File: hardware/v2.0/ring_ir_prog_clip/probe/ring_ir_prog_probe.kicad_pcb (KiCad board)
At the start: 2 copper layers, 14 x 29 mm, 11 parts, among them J1 AVR_ISP_6, J2 GND_lead_to_anvil, P1 Pogo TP1 PB0, P2 Pogo TP2 PB1, P3 Pogo TP3 PB2, P4 Pogo TP4 PB3, P5 Pogo TP5 PB4, P6 Pogo TP6 PB5, P9 Pogo TP9 VCC

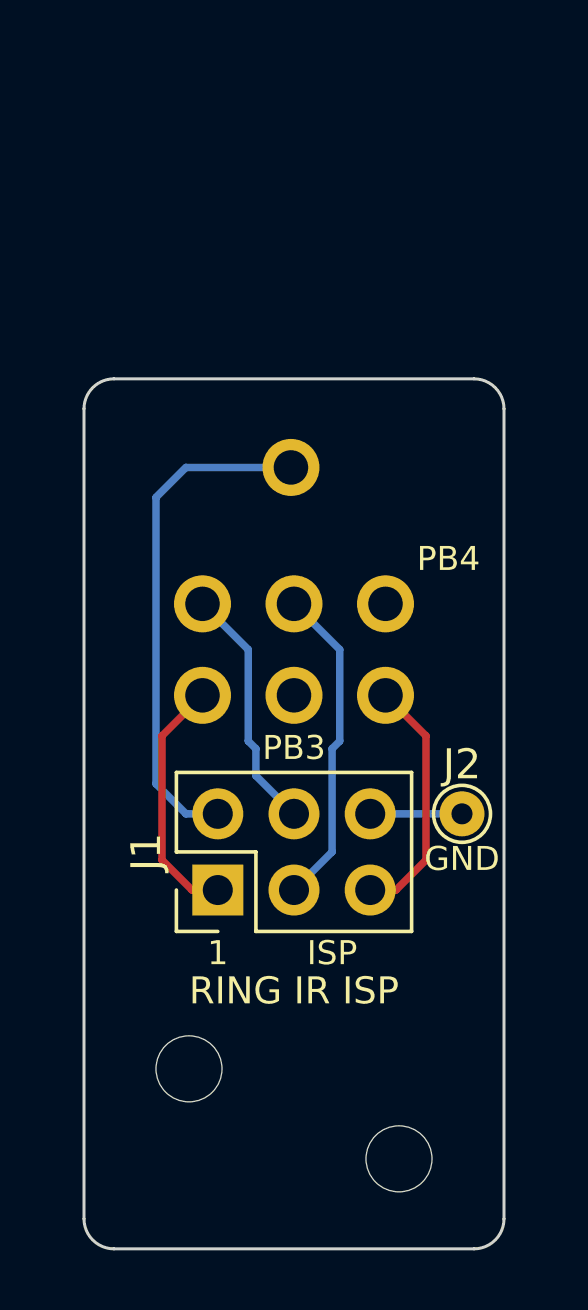
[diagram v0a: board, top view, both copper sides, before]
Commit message: IR prog clip: estimated clip dimensions and FreeCAD virtual fit check
Co-authored-by: Copilot <223556219+Copilot@users.noreply.github.com>
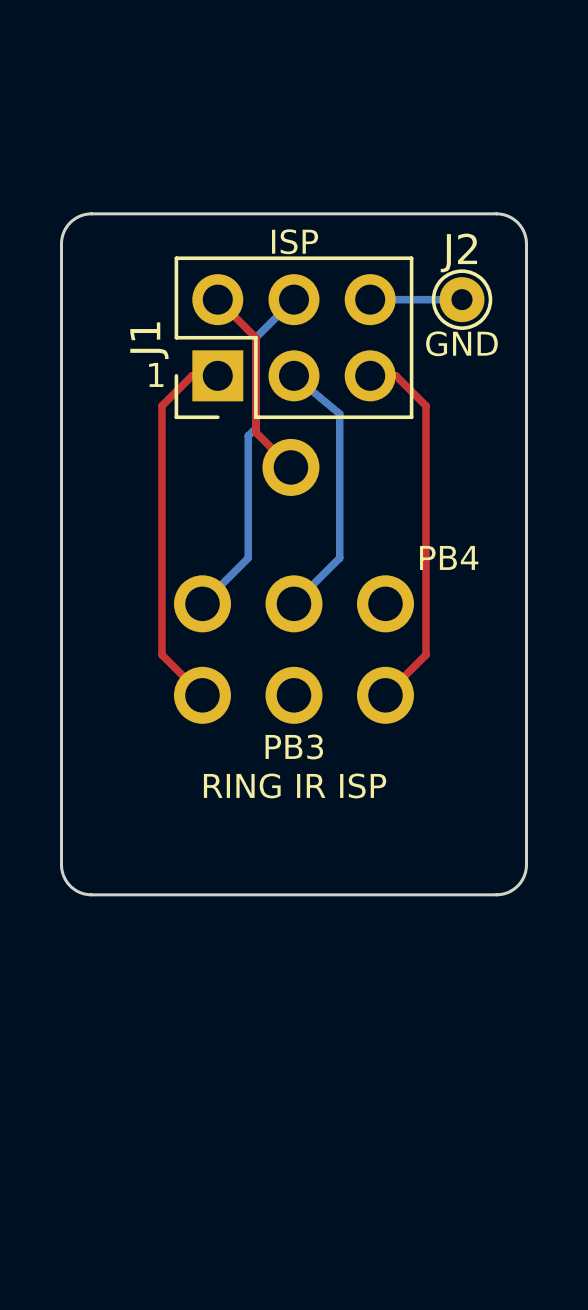
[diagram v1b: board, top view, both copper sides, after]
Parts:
- H1, H2: value MountingHole_2.2mm_M2 -> M2_Slot_Clip_Jaw; footprint MountingHole:MountingHole_2.2mm_M2 -> ring_ir_prog_clip:M2_Slot_Clip_Jaw
- moved J2 17.1 mm to (155.6, 89.9)
- moved J1 17.1 mm to (147.5, 92.4)
- moved H2 10.4 mm to (154.5, 108.1)
- moved H1 7.47 mm to (145.5, 108.1)
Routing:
- net /VCC: track 16.9 -> 6.60 mm
- net /PB5: track 8.32 -> 12.5 mm
- net /PB1: track 8.32 -> 12.5 mm
- net /PB0: track 8.26 -> 11.4 mm
- net /PB2: track 10.8 -> 8.95 mm
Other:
- board size 14 x 29 mm -> 15.5 x 22.7 mm
- board text added: "KIT JAW UNMEASURED"
- board text added: "UPPER JAW TIP (EST)"
- board text removed: "KIT HOLES UNMEASURED"

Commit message: Use SMD ISP header and STEP-based clip assembly renders
Regenerate checked clip PCBs, 2D drawings, actual STEP assemblies and assembly media. Document IR ISP wiring, the anvil ground return and target-specific SWD voltage-reference requirements.

Co-authored-by: Copilot <223556219+Copilot@users.noreply.github.com>
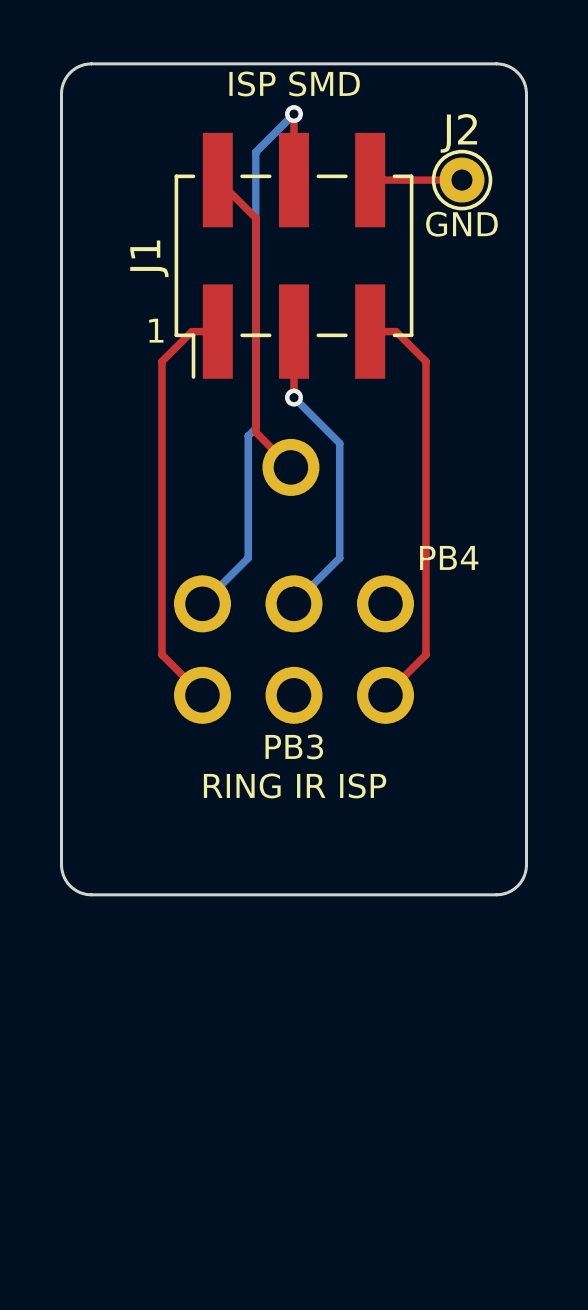
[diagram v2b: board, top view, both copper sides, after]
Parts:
- J1: value AVR_ISP_6 -> AVR_ISP_6_SMD; footprint Connector_PinHeader_2.54mm:PinHeader_2x03_P2.54mm_Vertical -> Connector_PinHeader_2.54mm:PinHeader_2x03_P2.54mm_Vertical_SMD
- moved J1 4.74 mm to (150.0, 88.4)
- moved J2 3.98 mm to (155.6, 85.9)
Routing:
- net /PB0: track 11.4 -> 19.8 mm, vias 0 -> 1
- net /VCC: track 6.60 -> 10.6 mm
- net /PB5: track 12.5 -> 14.0 mm
- net /PB1: track 12.5 -> 14.0 mm
- net /PB2: track 8.95 -> 10.3 mm, vias 0 -> 1
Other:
- board size 15.5 x 22.7 mm -> 15.5 x 27.7 mm
- board text added: "ISP SMD"
- board text removed: "ISP"
